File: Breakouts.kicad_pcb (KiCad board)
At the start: 2 copper layers, 1 part, among them U1 ESP-07

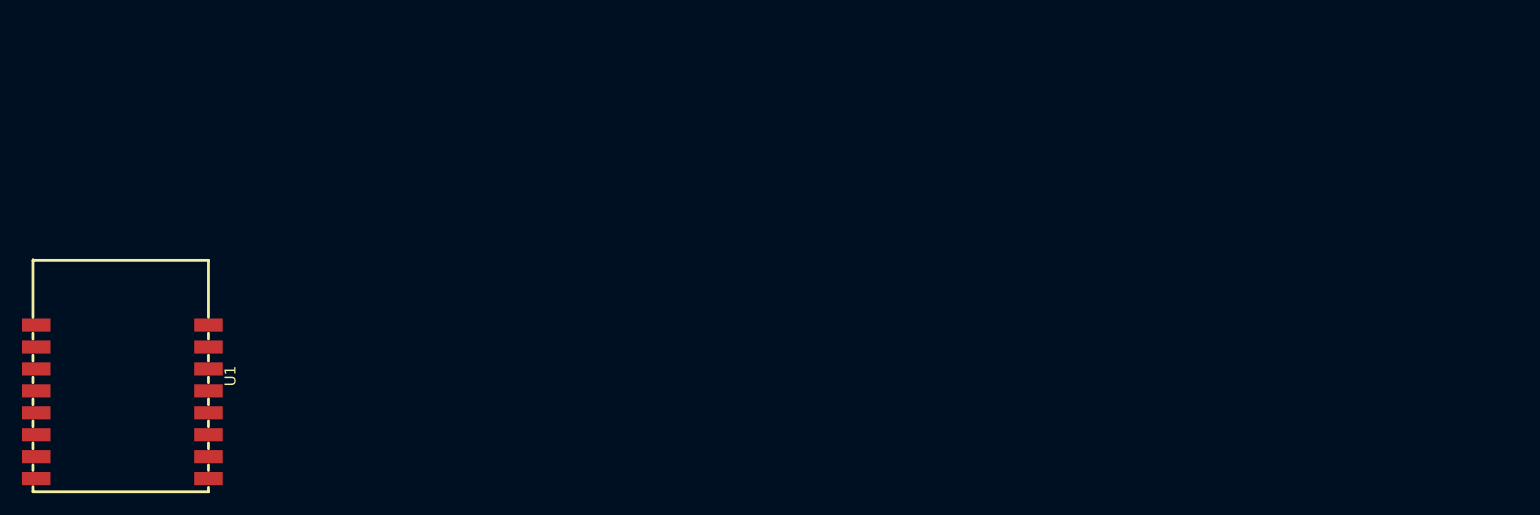
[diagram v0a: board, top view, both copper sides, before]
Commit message: Add AMS117
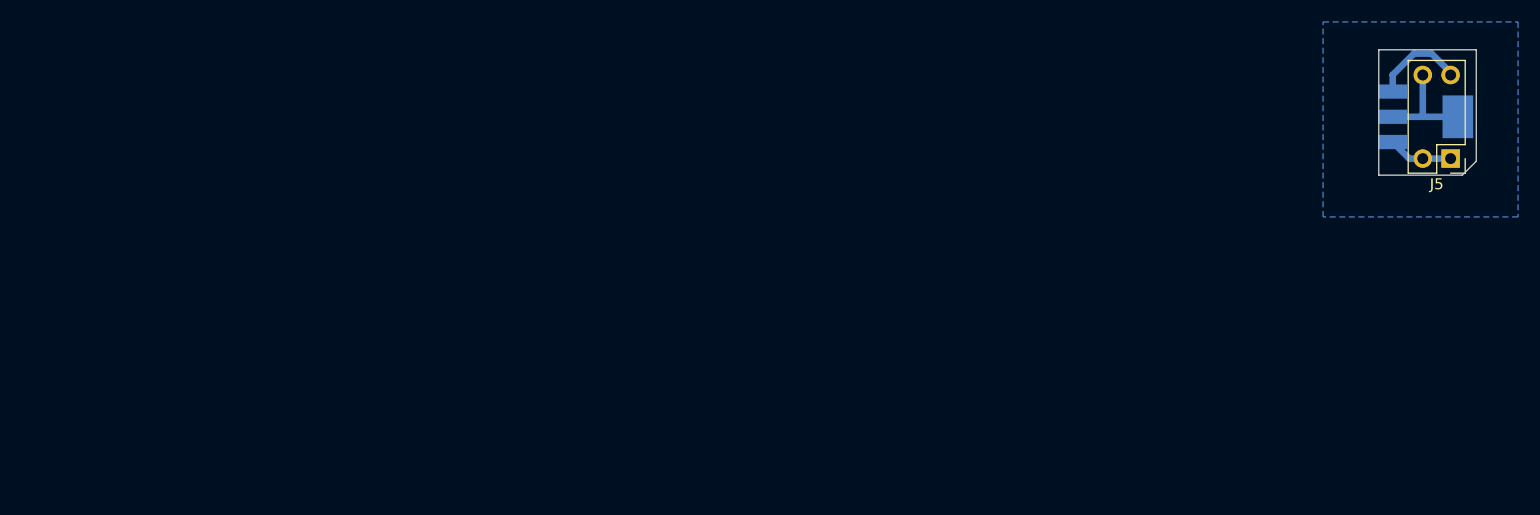
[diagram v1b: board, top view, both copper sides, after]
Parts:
- removed U1: ESP-07, jlc_footprints:WIFIM-SMD_ESP-07
- added J5: Conn_02x04_Odd_Even, Connector_PinHeader_2.54mm:PinHeader_2x04_P2.54mm_Vertical, F.Cu at (223.7, 35.3)
- added U2: AMS1117-3_3, jlc_footprints:SOT-223-3_L6.5-W3.4-P2.30-LS7.0-BR, B.Cu at (221.4, 31.5)
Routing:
- net Net-(J5-Pin_8): track 0.00 -> 9.83 mm
- net Net-(J5-Pin_7): track 0.00 -> 8.54 mm
- net GND: track 0.00 -> 5.91 mm
- added copper zone on B.Cu, net GND
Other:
- board outline added: 8.9 x 11.4 mm

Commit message: Add preliminary esp07
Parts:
- added J1: Conn_01x08, Connector_PinHeader_2.54mm:PinHeader_1x08_P2.54mm_Vertical, B.Cu at (90.8, 48.3)
- added J2: Conn_01x08, Connector_PinHeader_2.54mm:PinHeader_1x08_P2.54mm_Vertical, B.Cu at (110.9, 66.1)
- added J3: Conn_01x08, Connector_PinHeader_2.54mm:PinHeader_1x08_P2.54mm_Vertical, F.Cu at (190.5, 48.3)
- added J4: Conn_01x08, Connector_PinHeader_2.54mm:PinHeader_1x08_P2.54mm_Vertical, F.Cu at (167.6, 66.0)
- added U1: ESP-07, jlc_footprints:WIFIM-SMD_ESP-07, B.Cu at (179.1, 57.0)
- added U3: ESP-12E, jlc_footprints:WIFIM-SMD_ESP-07, F.Cu at (98.4, 30.3)
- added U999999: ESP-12E, ESP8266:ESP-12E, F.Cu at (93.9, 50.5)
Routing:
- net Net-(J4-Pin_1): track 0.00 -> 4.43 mm
- net Net-(J3-Pin_8): track 0.00 -> 4.43 mm
- net Net-(J3-Pin_1): track 0.00 -> 4.29 mm
- net Net-(J4-Pin_8): track 0.00 -> 4.29 mm
- net Net-(J2-Pin_8): track 0.00 -> 4.28 mm
- net Net-(J3-Pin_7): track 0.00 -> 4.21 mm
- net Net-(J4-Pin_2): track 0.00 -> 4.21 mm
- net Net-(J1-Pin_1): track 0.00 -> 4.17 mm
- net Net-(J3-Pin_2): track 0.00 -> 4.07 mm
- net Net-(J4-Pin_7): track 0.00 -> 4.06 mm
- net Net-(J3-Pin_6): track 0.00 -> 3.99 mm
- net Net-(J4-Pin_3): track 0.00 -> 3.98 mm
- net Net-(J1-Pin_2): track 0.00 -> 3.95 mm
- net Net-(J2-Pin_7): track 0.00 -> 3.93 mm
- net Net-(J3-Pin_3): track 0.00 -> 3.85 mm
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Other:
- board size 8.9 x 11.4 mm -> 136.6 x 41.7 mm

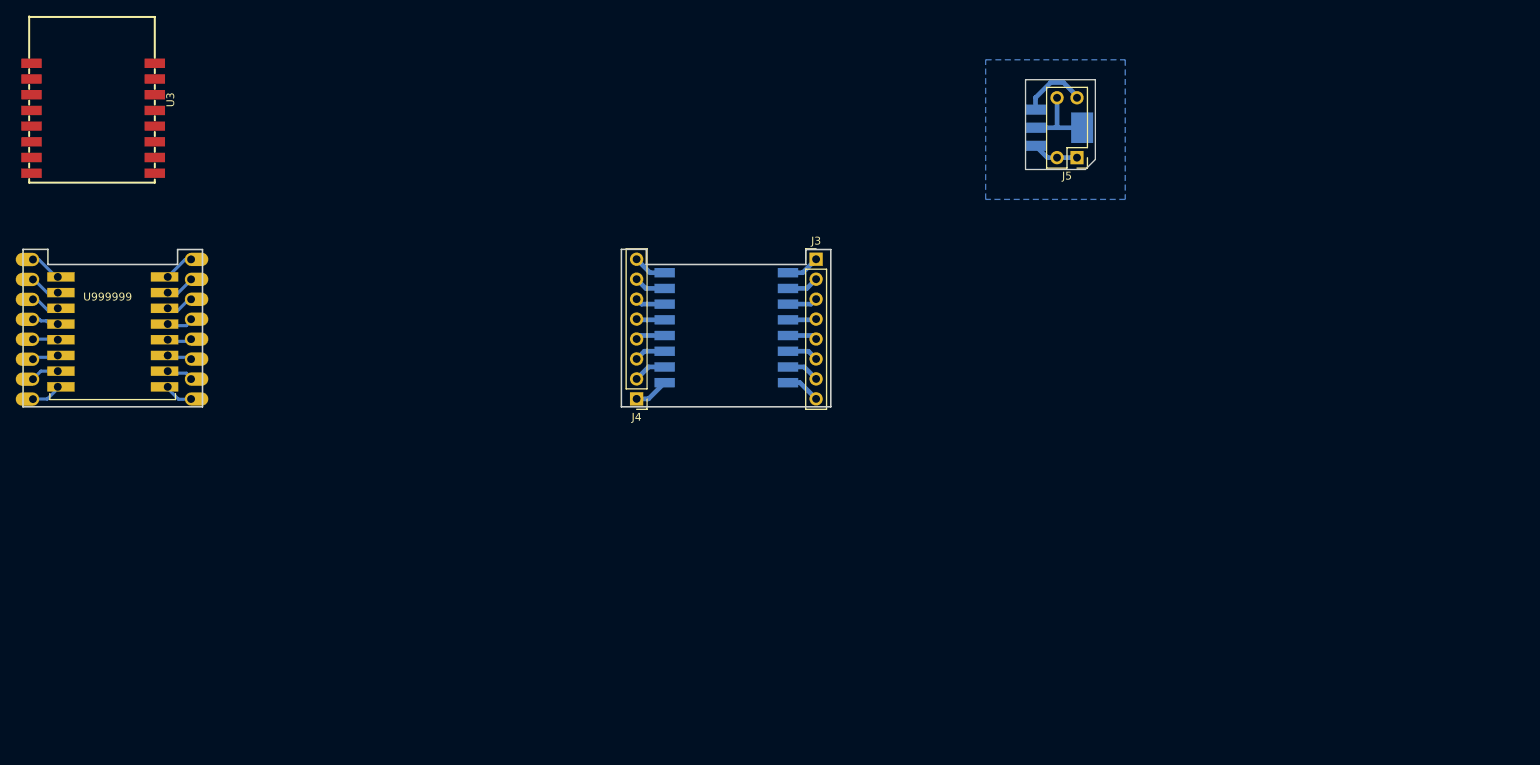
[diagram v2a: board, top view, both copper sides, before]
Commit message: Added relay breakout
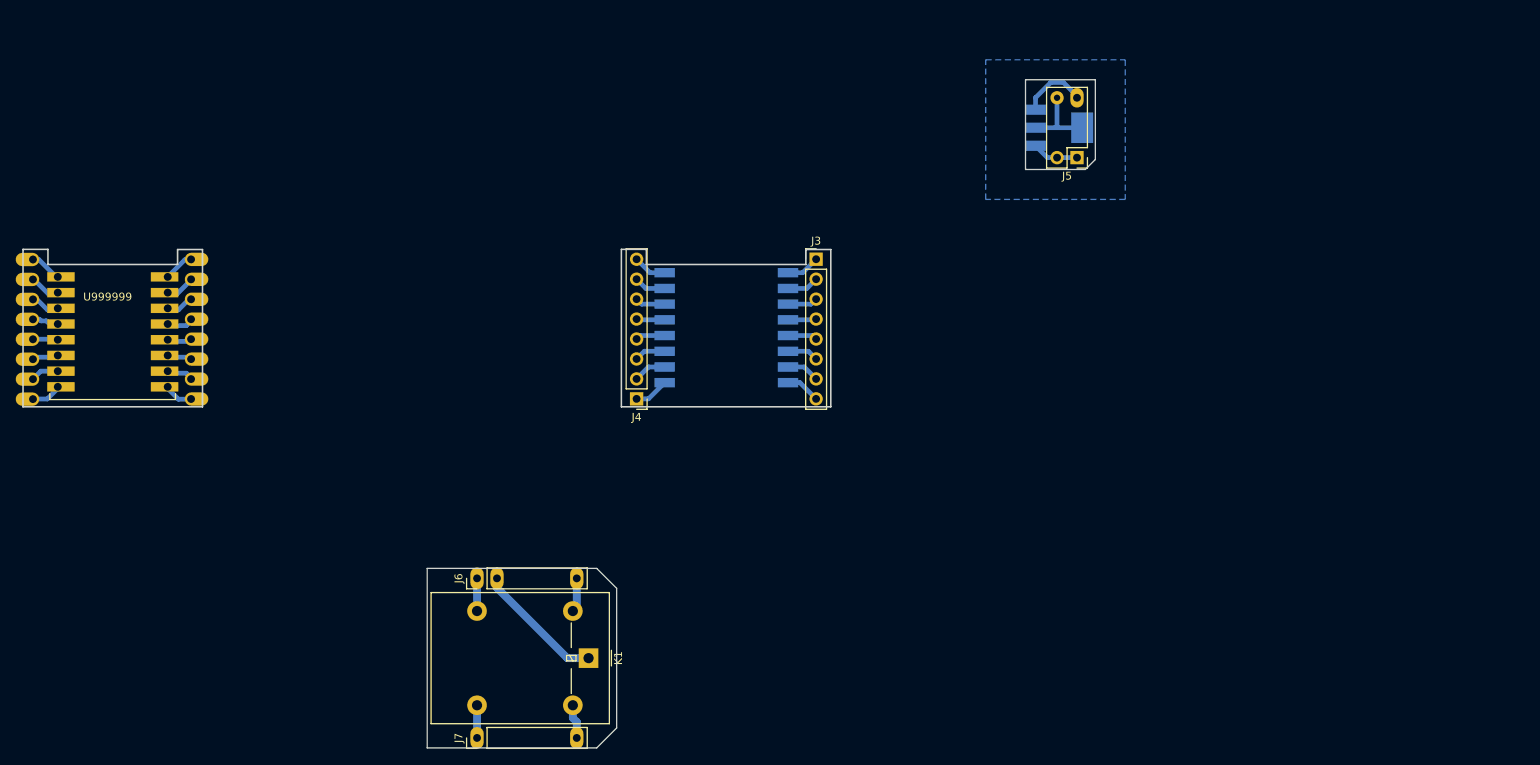
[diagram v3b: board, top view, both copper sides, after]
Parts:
- removed U3: ESP-12E, jlc_footprints:WIFIM-SMD_ESP-07
- added J6: Conn_01x06, Connector_PinHeader_2.54mm:PinHeader_1x06_P2.54mm_Vertical, F.Cu at (147.3, 88.9)
- added J7: Conn_01x06, Connector_PinHeader_2.54mm:PinHeader_1x06_P2.54mm_Vertical, F.Cu at (147.3, 109.2)
- added K1: G5LE-1, Relay_THT:Relay_SPDT_Omron-G5LE-1, F.Cu at (161.5, 99.1)
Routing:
- net Net-(J6-Pin_2): track 0.00 -> 16.6 mm
- net Net-(J7-Pin_6): track 0.00 -> 4.37 mm
- net Net-(J6-Pin_6): track 0.00 -> 4.37 mm
- net Net-(J7-Pin_1): track 0.00 -> 4.16 mm
- net Net-(J6-Pin_1): track 0.00 -> 4.16 mm
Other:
- board size 136.6 x 41.7 mm -> 136.6 x 85.1 mm

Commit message: Add audio jack
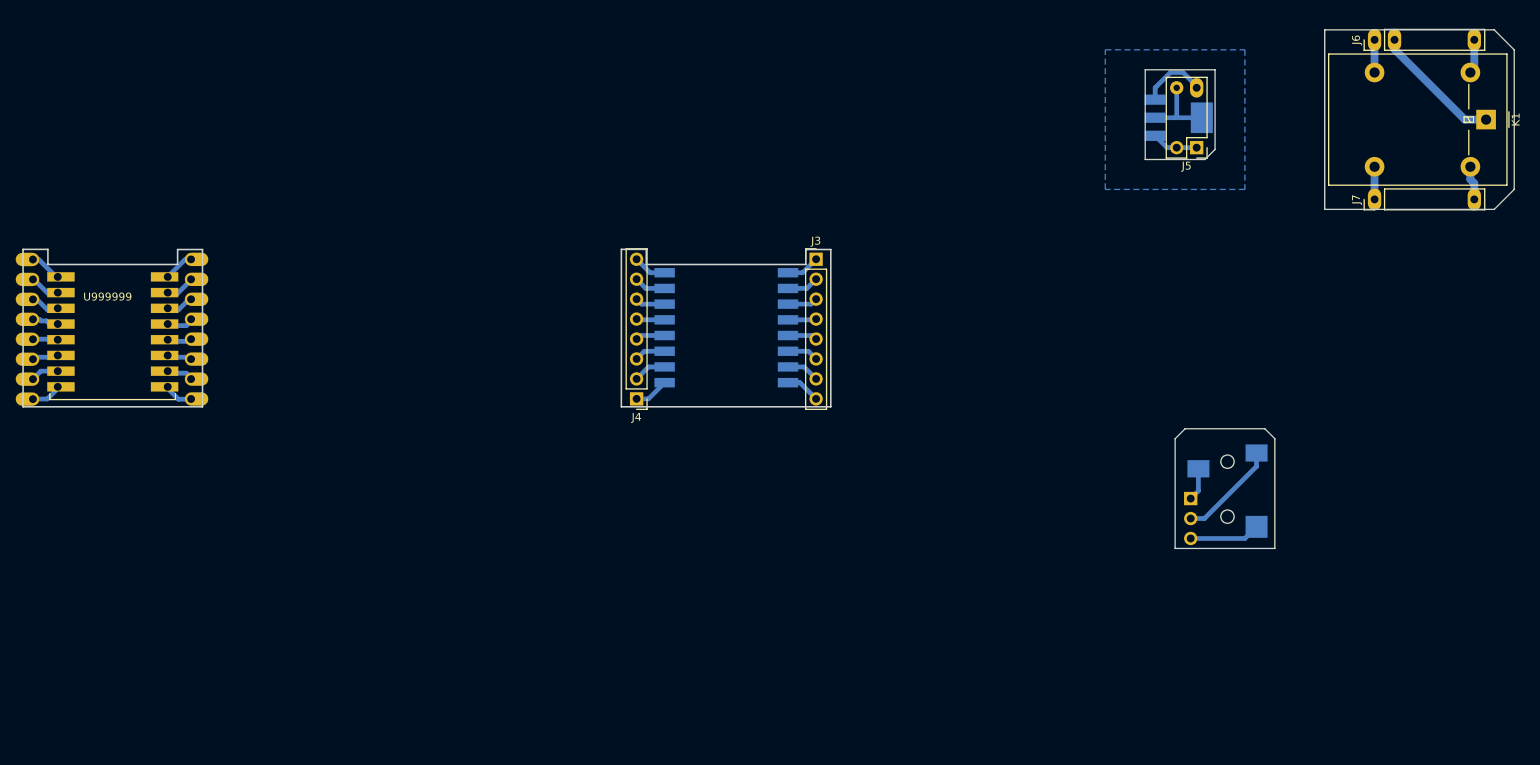
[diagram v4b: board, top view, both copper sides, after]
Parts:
- added J8: AudioJack3, Connector_Audio:Jack_3.5mm_CUI_SJ-3523-SMT_Horizontal, B.Cu at (242.9, 76.5)
- added J9: Conn_01x03, Connector_PinHeader_2.54mm:PinHeader_1x03_P2.54mm_Vertical, B.Cu at (238.2, 78.7)
- moved J6 133.3 mm to (261.6, 20.3)
- moved J7 133.3 mm to (261.6, 40.6)
- moved K1 133.3 mm to (275.8, 30.5)
- moved J5 15.3 mm to (239.0, 34.0)
- moved U2 15.3 mm to (236.6, 30.2)
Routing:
- net Net-(J9-Pin_2): track 0.00 -> 12.8 mm
- net Net-(J9-Pin_3): track 0.00 -> 8.99 mm
- net Net-(J9-Pin_1): track 0.00 -> 4.21 mm
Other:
- board size 136.6 x 85.1 mm -> 189.9 x 66 mm
